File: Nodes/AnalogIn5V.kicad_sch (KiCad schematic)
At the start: 78 parts, among them T12 Conn_01x01, T13 Conn_01x01, T14 Conn_01x01, T15 Conn_01x01, T16 Conn_01x01, T17 Conn_01x01, T18 Conn_01x01, U6 LM358BAIDR, U7 LM358BAIDR, U8 LM358BAIDR, U9 LM358BAIDR

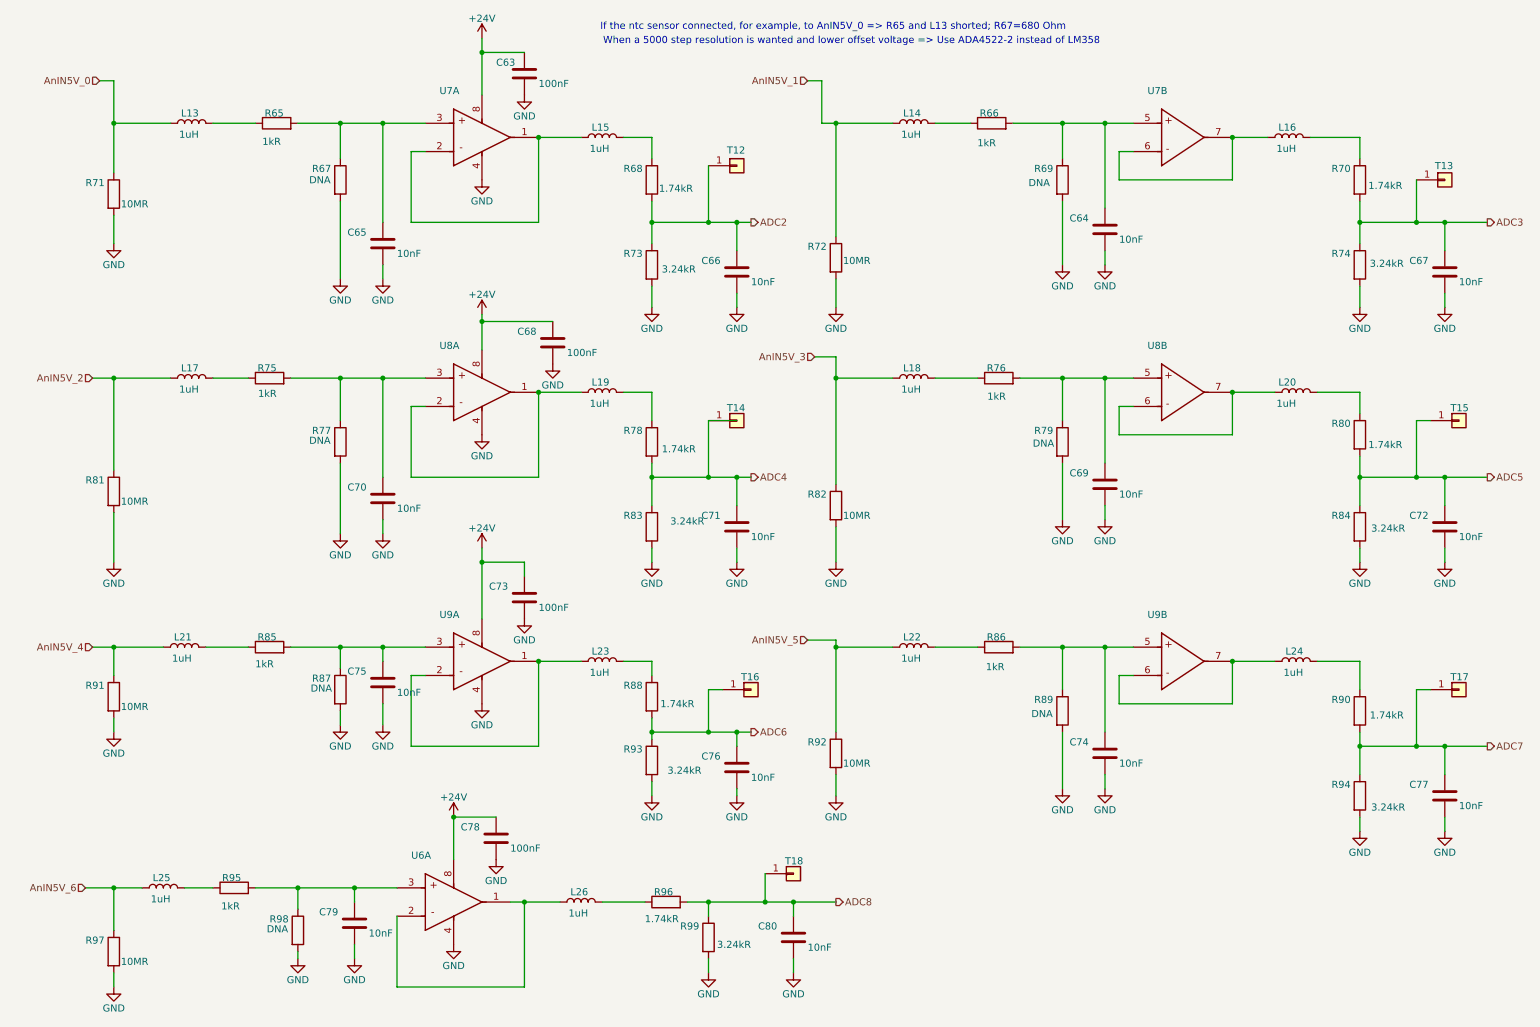
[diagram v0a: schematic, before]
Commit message: Nodes v2.1.2 Improved
- Improved schematic design
- Added two 4.7 uF caps according to the datasheets of the microchips
- Other small changes
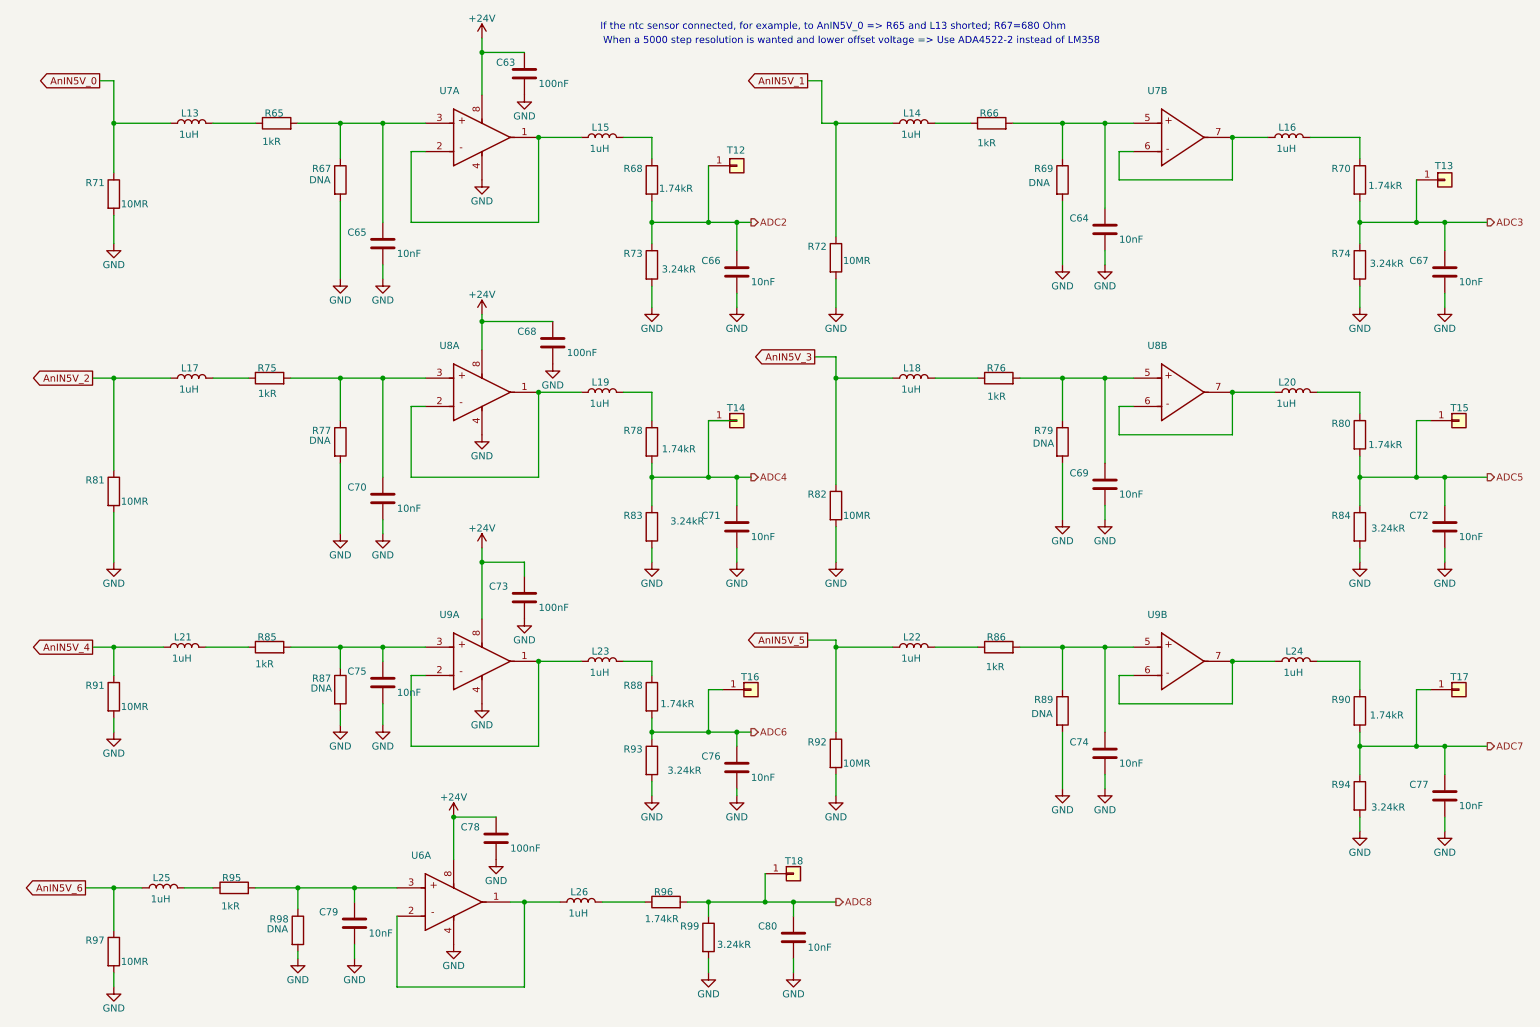
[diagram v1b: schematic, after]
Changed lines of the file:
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@@
 		)
 	)
-	(hierarchical_label "AnIN5V_5"
-		(shape input)
+	(global_label "AnIN5V_5"
+		(shape output)
 		(at 153.67 125.73 180)
 		(fields_autoplaced yes)
@@
 			(justify right)
 		)
-	)
-	(hierarchical_label "AnIN5V_1"
-		(shape input)
+		(property "Intersheetrefs" "${INTERSHEET_REFS}"
+			(at 142.0367 125.73 0)
+			(effects
+				(font
+					(size 1.27 1.27)
+				)
+				(justify right)
+				(hide yes)
+			)
+		)
+	)
+	(global_label "AnIN5V_4"
+		(shape output)
+		(at 25.4 127 180)
+		(fields_autoplaced yes)
+		(effects
+			(font
+				(size 1.27 1.27)
+			)
+			(justify right)
+		)
+		(property "Intersheetrefs" "${INTERSHEET_REFS}"
+			(at 13.7667 127 0)
+			(effects
+				(font
+					(size 1.27 1.27)
+				)
+				(justify right)
+				(hide yes)
+			)
+		)
+	)
+	(global_label "AnIN5V_2"
+		(shape output)
+		(at 25.4 78.74 180)
+		(fields_autoplaced yes)
+		(effects
+			(font
+				(size 1.27 1.27)
+			)
+			(justify right)
+		)
+		(property "Intersheetrefs" "${INTERSHEET_REFS}"
+			(at 13.7667 78.74 0)
+			(effects
+				(font
+					(size 1.27 1.27)
+				)
+				(justify right)
+				(hide yes)
+			)
+		)
+	)
+	(global_label "AnIN5V_3"
+		(shape output)
+		(at 154.94 74.93 180)
+		(fields_autoplaced yes)
+		(effects
+			(font
+				(size 1.27 1.27)
+			)
+			(justify right)
+		)
+		(property "Intersheetrefs" "${INTERSHEET_REFS}"
+			(at 143.3067 74.93 0)
+			(effects
+				(font
+					(size 1.27 1.27)
+				)
+				(justify right)
+				(hide yes)
+			)
+		)
+	)
+	(global_label "AnIN5V_1"
+		(shape output)
 		(at 153.67 25.4 180)
 		(fields_autoplaced yes)
@@
 			(justify right)
 		)
+		(property "Intersheetrefs" "${INTERSHEET_REFS}"
+			(at 142.0367 25.4 0)
+			(effects
+				(font
+					(size 1.27 1.27)
+				)
+				(justify right)
+				(hide yes)
+			)
+		)
+	)
+	(global_label "AnIN5V_0"
+		(shape output)
+		(at 26.67 25.4 180)
+		(fields_autoplaced yes)
+		(effects
+			(font
+				(size 1.27 1.27)
+			)
+			(justify right)
+		)
+		(property "Intersheetrefs" "${INTERSHEET_REFS}"
+			(at 15.0367 25.4 0)
+			(effects
+				(font
+					(size 1.27 1.27)
+				)
+				(justify right)
+				(hide yes)
+			)
+		)
+	)
+	(global_label "AnIN5V_6"
+		(shape output)
+		(at 24.13 170.18 180)
+		(fields_autoplaced yes)
+		(effects
+			(font
+				(size 1.27 1.27)
+			)
+			(justify right)
+		)
+		(property "Intersheetrefs" "${INTERSHEET_REFS}"
+			(at 12.4967 170.18 0)
+			(effects
+				(font
+					(size 1.27 1.27)
+				)
+				(justify right)
+				(hide yes)
+			)
+		)
 	)
 	(hierarchical_label "ADC6"
@@
 		)
 	)
-	(hierarchical_label "AnIN5V_6"
-		(shape input)
-		(at 24.13 170.18 180)
-		(fields_autoplaced yes)
-		(effects
-			(font
-				(size 1.27 1.27)
-			)
-			(justify right)
-		)
-	)
-	(hierarchical_label "AnIN5V_2"
-		(shape input)
-		(at 25.4 78.74 180)
-		(fields_autoplaced yes)
-		(effects
-			(font
-				(size 1.27 1.27)
-			)
-			(justify right)
-		)
-	)
-	(hierarchical_label "AnIN5V_3"
-		(shape input)
-		(at 154.94 74.93 180)
-		(fields_autoplaced yes)
-		(effects
-			(font
-				(size 1.27 1.27)
-			)
-			(justify right)
-		)
-	)
 	(hierarchical_label "ADC2"
 		(shape output)
@@
 		)
 	)
-	(hierarchical_label "AnIN5V_4"
-		(shape input)
-		(at 25.4 127 180)
-		(fields_autoplaced yes)
-		(effects
-			(font
-				(size 1.27 1.27)
-			)
-			(justify right)
-		)
-	)
 	(hierarchical_label "ADC8"
 		(shape output)
@@
 		)
 	)
-	(hierarchical_label "AnIN5V_0"
-		(shape input)
-		(at 26.67 25.4 180)
-		(fields_autoplaced yes)
-		(effects
-			(font
-				(size 1.27 1.27)
-			)
-			(justify right)
-		)
-	)

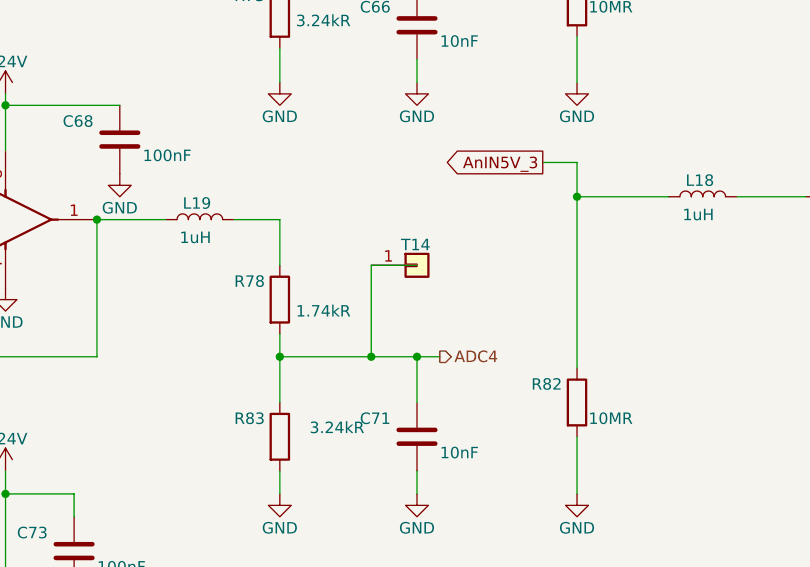
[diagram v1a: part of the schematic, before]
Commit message: Nodes v2.2
- This version not compatible with BOB v.2.1.2 and older!
- Completely new layout design
- New power supply system with new voltage regulators
- New microchip STM32G431RBTx for the Analog Node
- New connection system (instead of 18 pin headers now 8 pin and pins were grouped by functions)
- Reduced size of the board by 5%
- Removed power switch for the Analog Node (because this functionality is now provided by a separate voltage regulator. for a more stable voltage)
- Removable ground from the holes added
- Layer numbers added
- Small improvements of the components information were made
- New oscillator for the Nodes
- Removed CAN1, so now only one CAN connection due to the capabilities of the new microchip
- Other small changes and fixes on the schematic and design
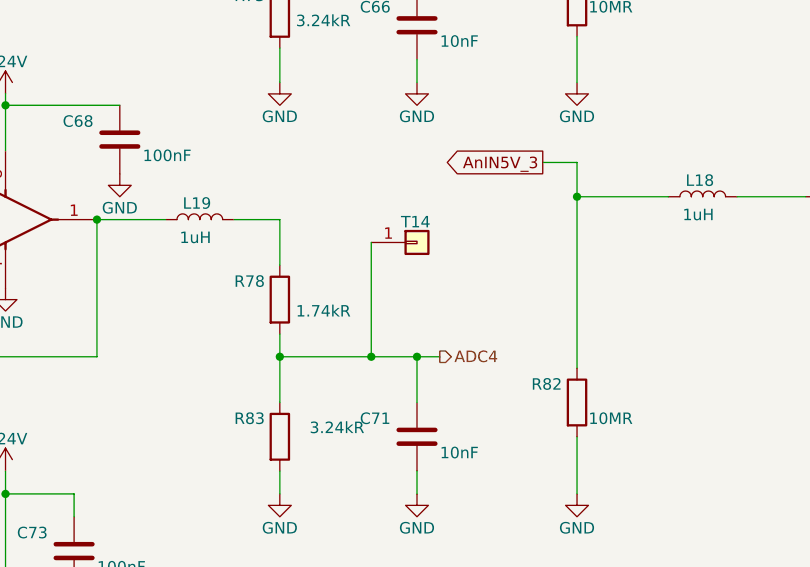
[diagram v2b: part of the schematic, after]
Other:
- moved on the sheet: T14

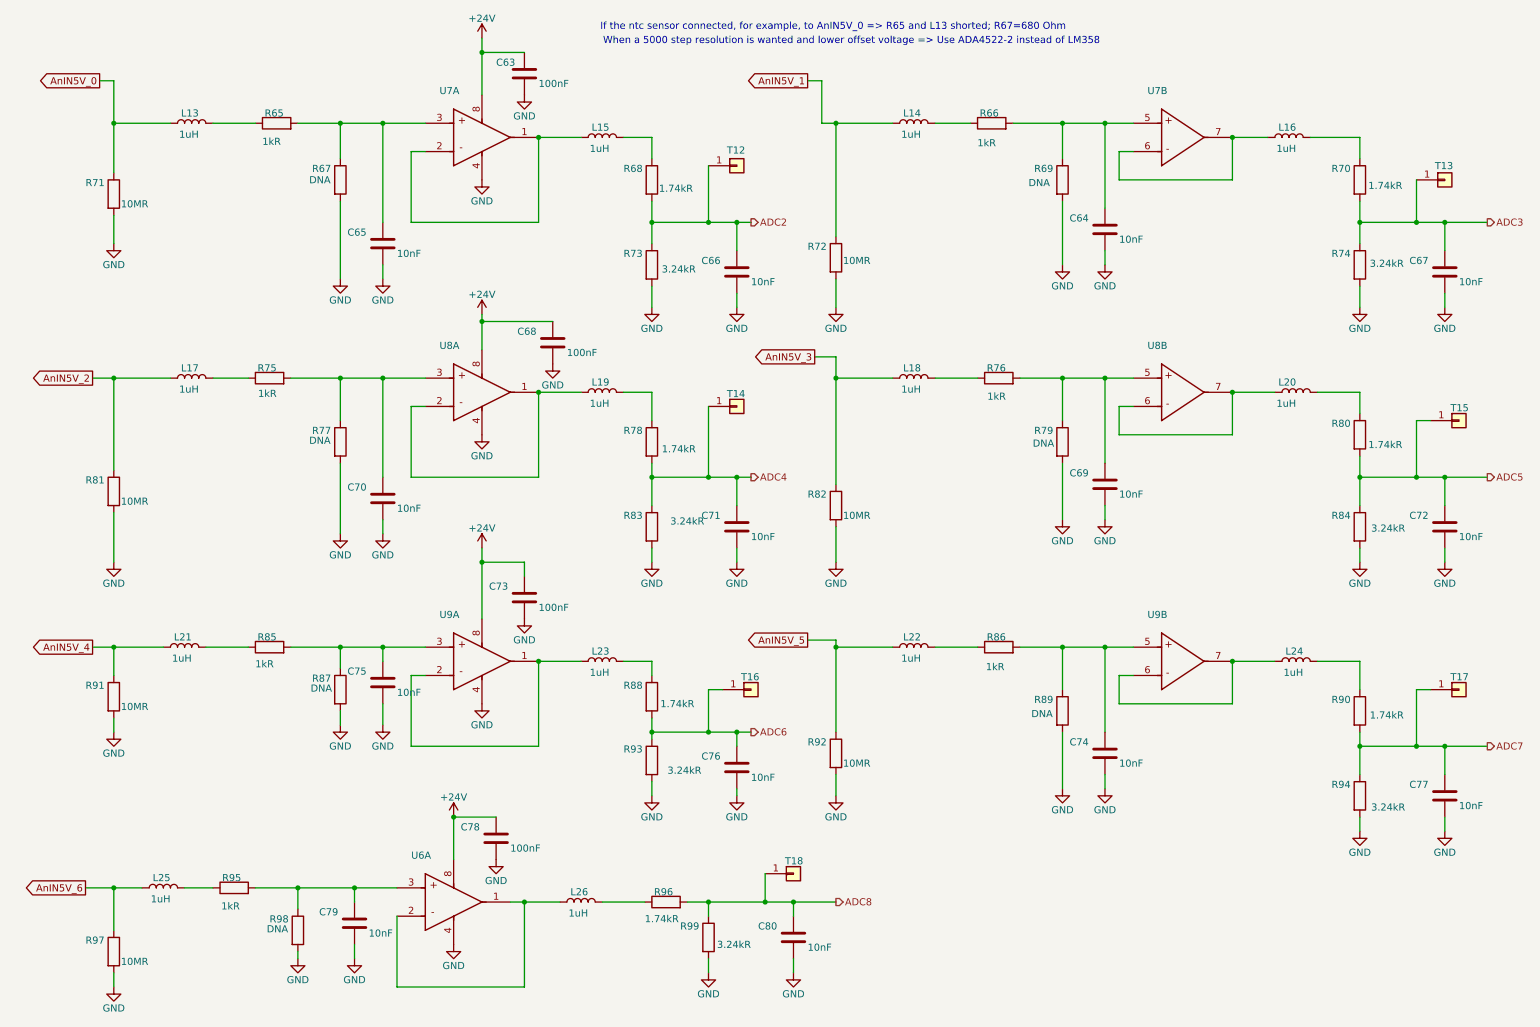
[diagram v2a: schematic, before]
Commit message: Nodes v2.2.5
- New High-Side Driver (Same footprint, just new info)
- Two resistors added for 3V3 Filters, which can be used to implement voltage divider
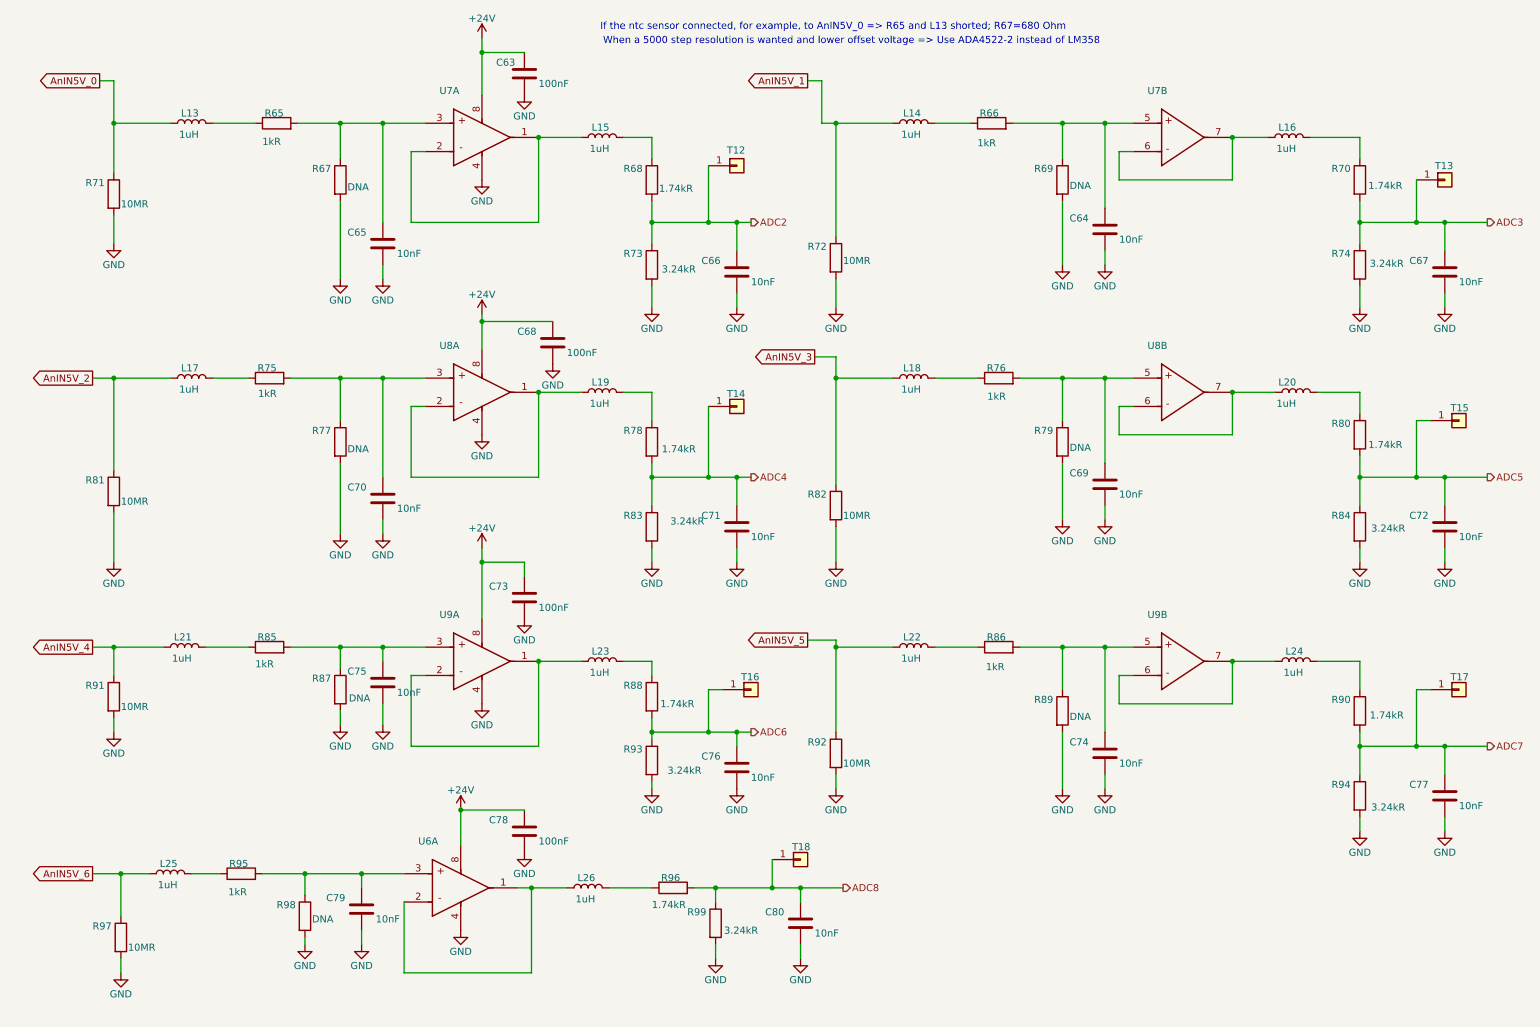
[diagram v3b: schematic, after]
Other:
- moved on the sheet: C78, C79, C80, L25, L26, R95, R96, R97, R98, R99, T18, U6A
